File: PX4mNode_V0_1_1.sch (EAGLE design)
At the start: 135 parts, among them J201 DF13C-6P-1.25V, J202 DF13C-6P-1.25V, J203 DF13C-6P-1.25V, J301 DF13C-4P-1.25V, J401 DF13C-7P-1.25V, J402 DF13-4P-1.25V, J403 DF13C-4P-1.25V, J404 DF13C-4P-1.25V, J405 DF13C-4P-1.25V, J801 DF13C-3P-1.25V, M3_MOUNT1101 MOUNT-HOLE3.1MM, M3_MOUNT1102 MOUNT-HOLE3.1MM, M3_MOUNT1103 MOUNT-HOLE3.1MM, M3_MOUNT1104 MOUNT-HOLE3.1MM, U101 STM32F4X7VX, U401 MAX3051, U402 MAX3051, X101 3.2x2.5 mm / 24 MHz / 15 ppm

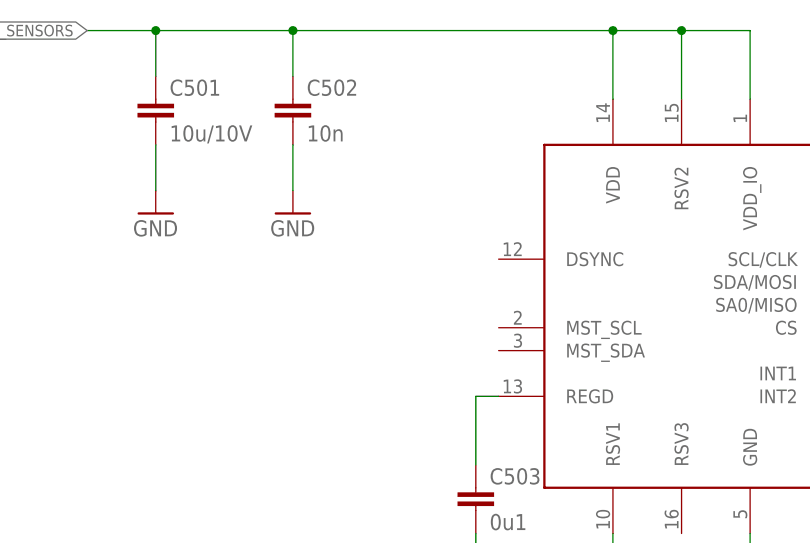
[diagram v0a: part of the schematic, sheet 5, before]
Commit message: Patched MAX21100 DRDY to MAG_DRDY
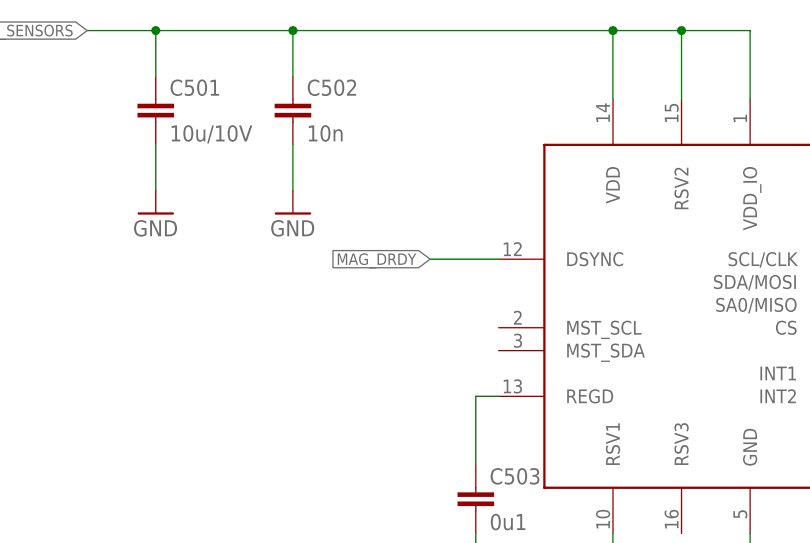
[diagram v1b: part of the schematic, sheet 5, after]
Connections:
- net MAG_DRDY: now also U$501.DSYNC
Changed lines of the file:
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@@
+</segment>
+</net>
+<net name="MAG_DRDY" class="0">
+<segment>
+<pinref part="U$501" gate="A" pin="DSYNC"/>
+<wire x1="88.9" y1="76.2" x2="81.28" y2="76.2" width="0.1524" layer="91"/>
+<label x="81.28" y="76.2" size="1.27" layer="95" rot="R180" xref="yes"/>
 </segment>
 </net>

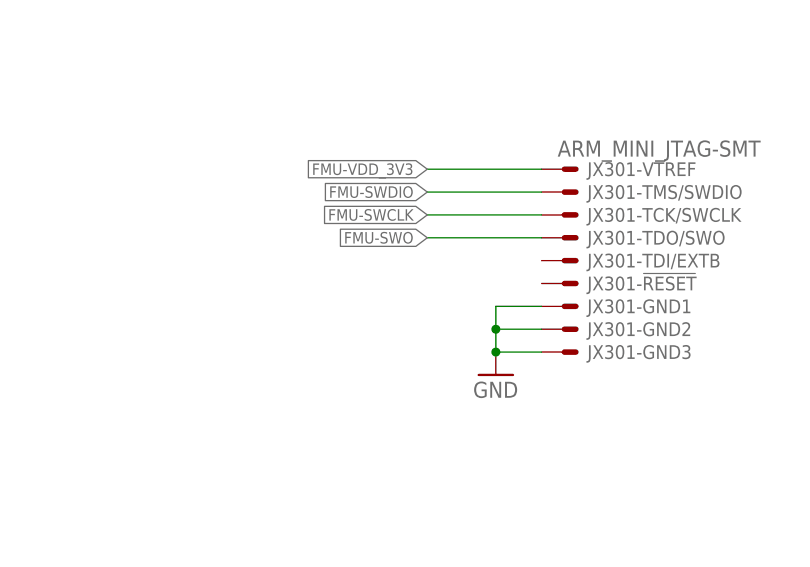
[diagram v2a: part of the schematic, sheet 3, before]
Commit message: Added nReset SWD connection to !FMU_RESET
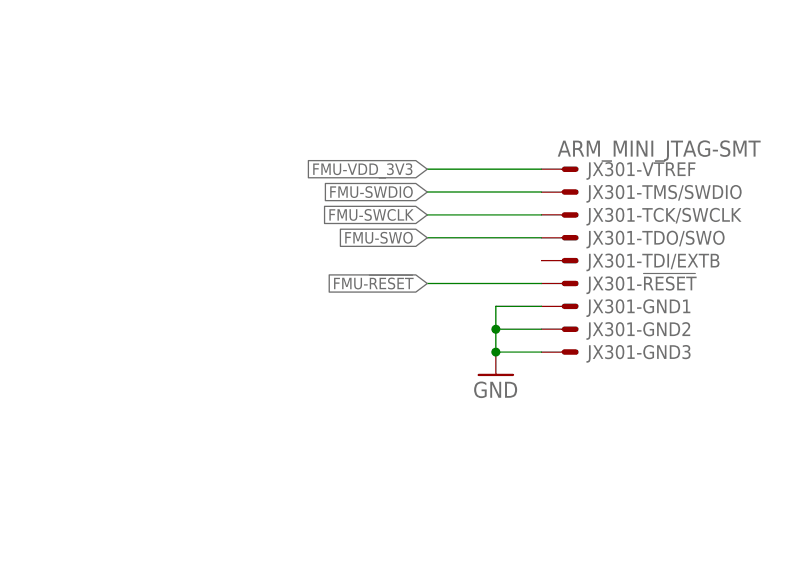
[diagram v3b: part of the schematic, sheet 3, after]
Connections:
- net FMU-!RESET: now also JX301-!RESET.S
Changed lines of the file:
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@@
+</segment>
+</net>
+<net name="FMU-!RESET" class="0">
+<segment>
+<label x="185.42" y="86.36" size="1.27" layer="95" rot="R180" xref="yes"/>
+<pinref part="JX301" gate="-!RESET" pin="S"/>
+<wire x1="185.42" y1="86.36" x2="198.12" y2="86.36" width="0.1524" layer="91"/>
 </segment>
 </net>

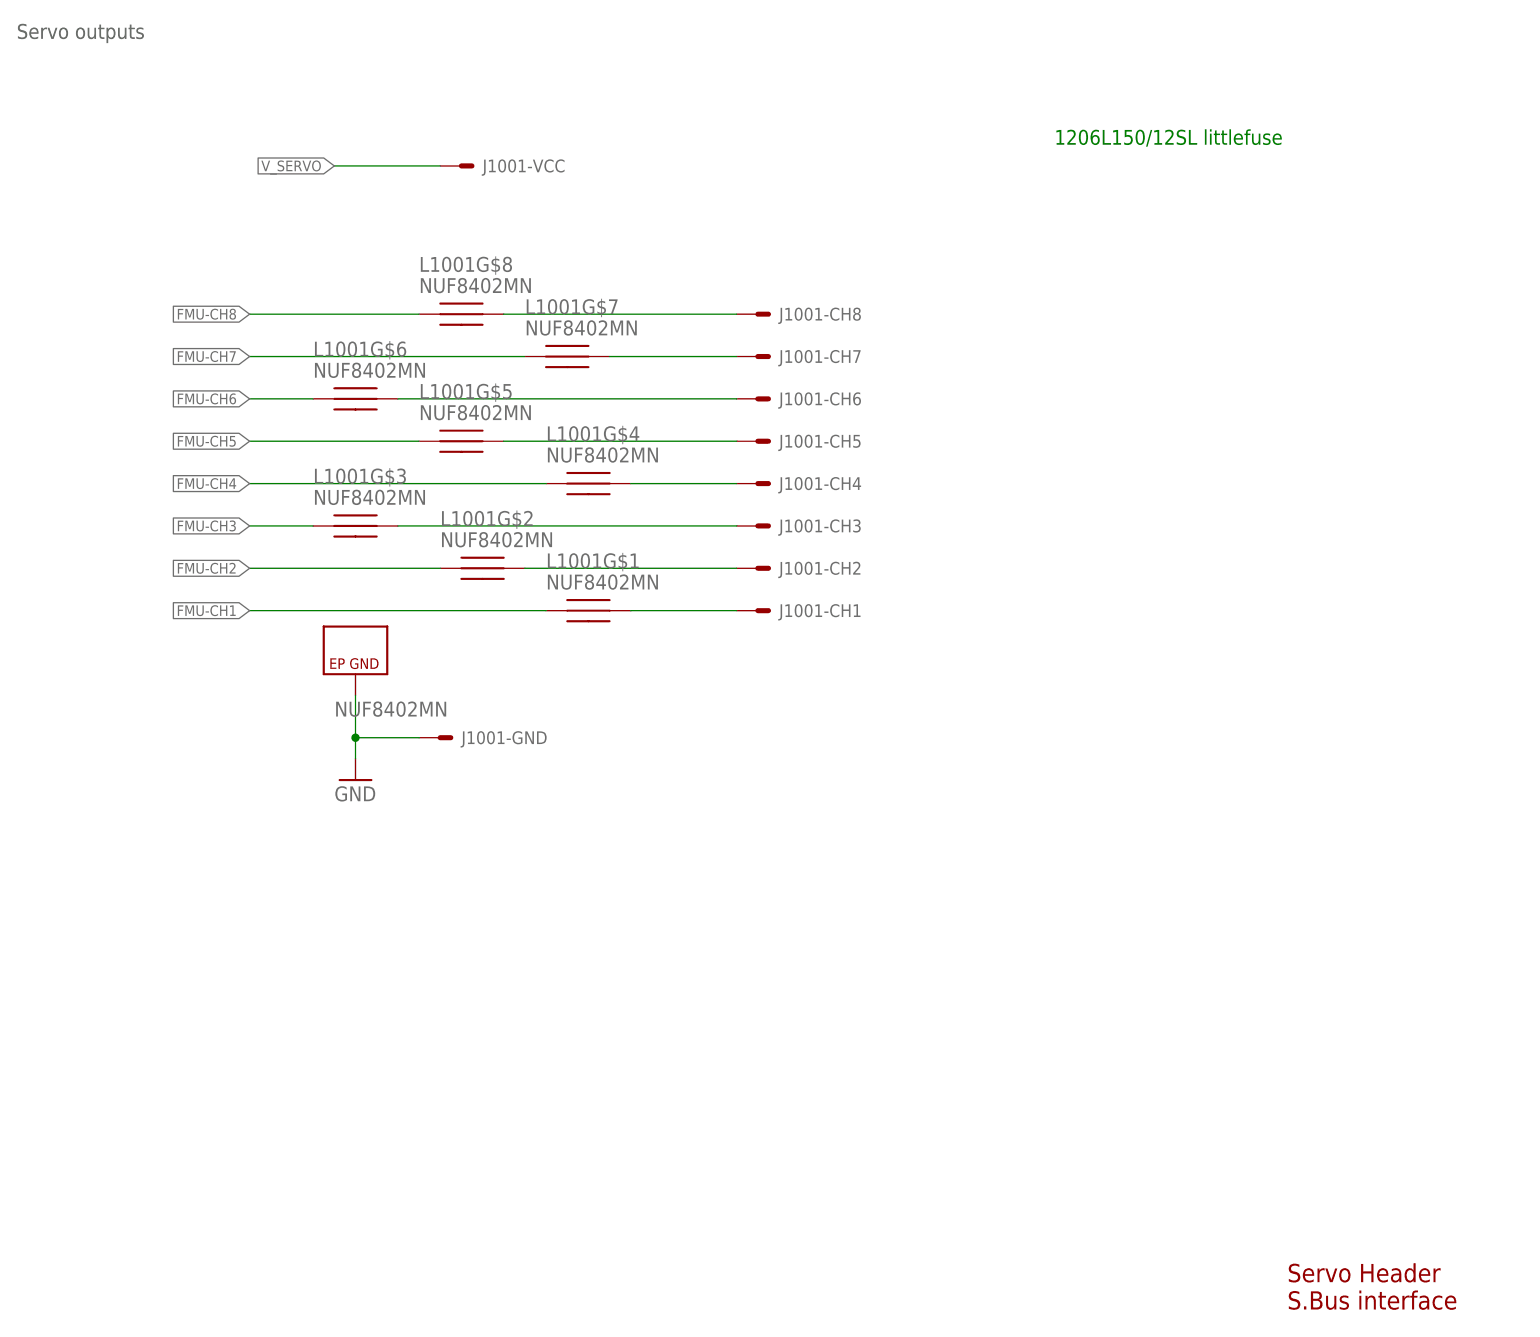
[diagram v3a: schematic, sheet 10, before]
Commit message: Added extra ground and power connections
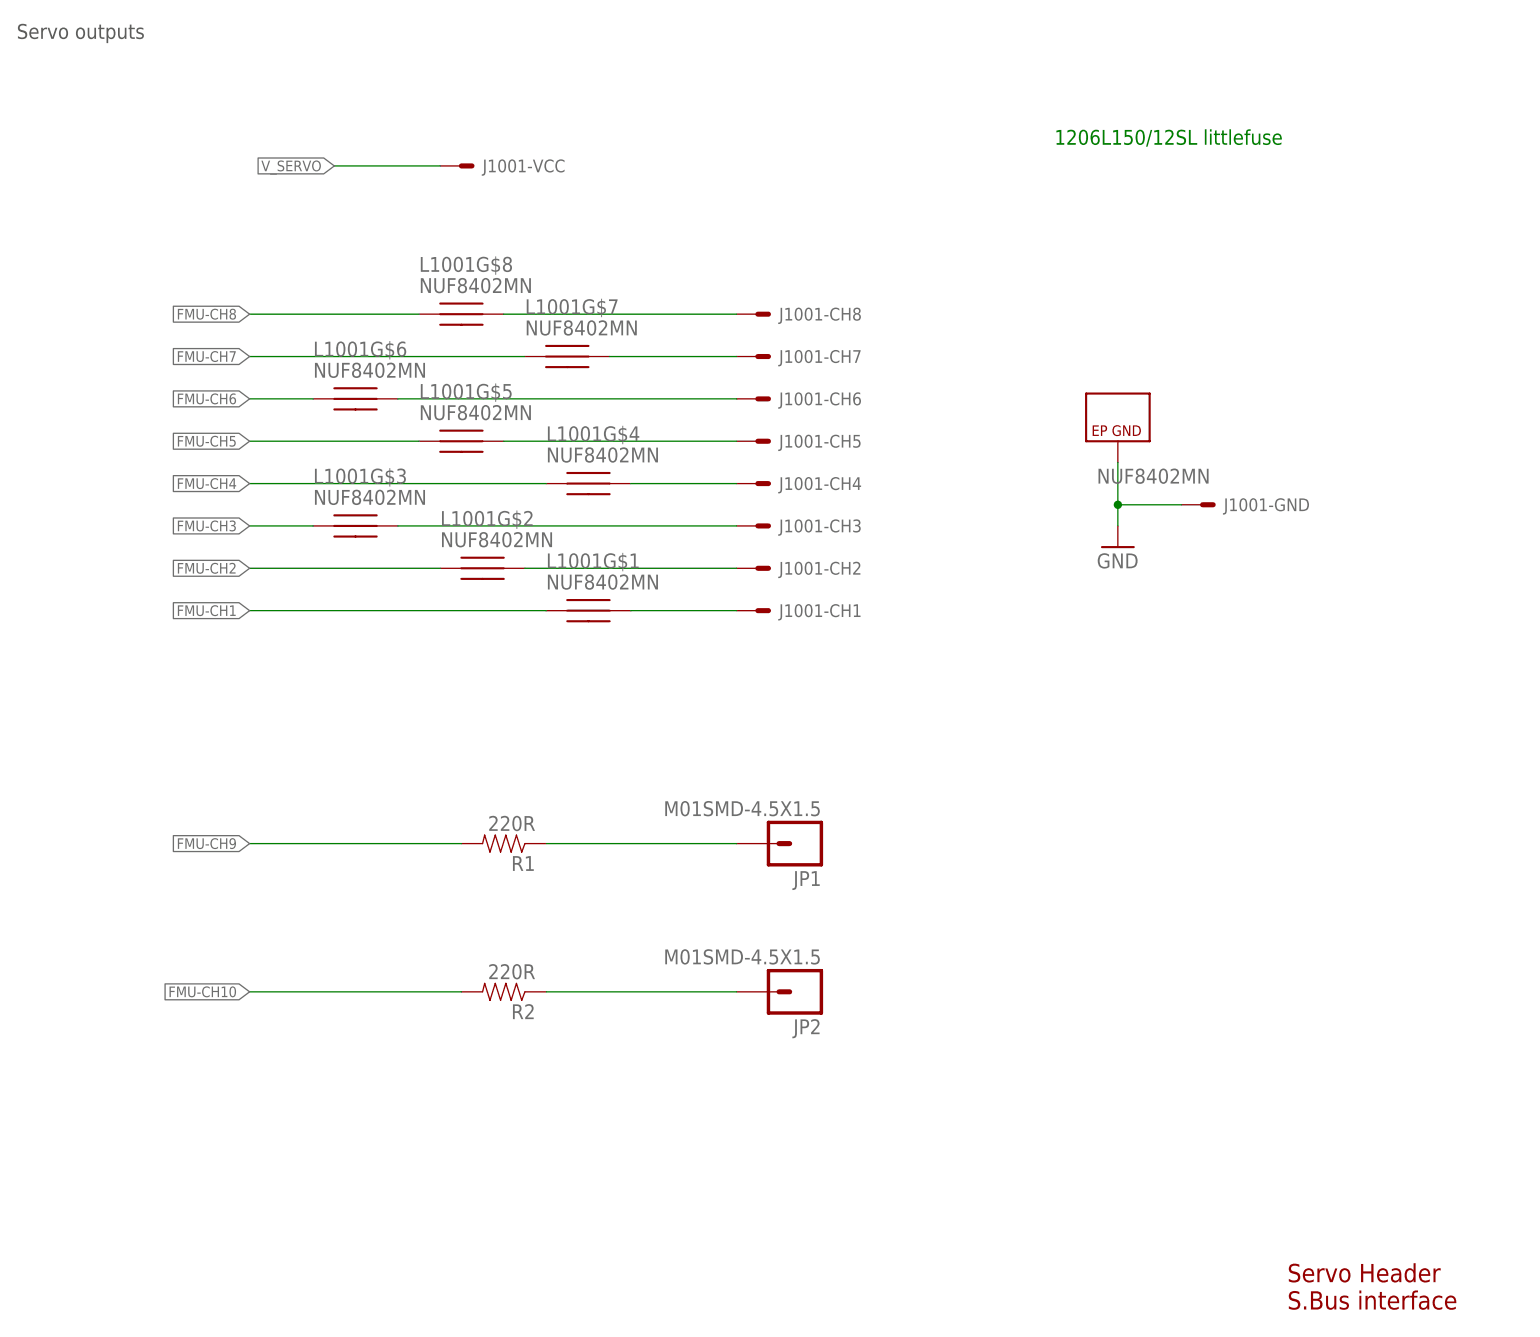
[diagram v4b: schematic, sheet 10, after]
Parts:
- added JP1, JP2, JP3: M01SMD-4.5X1.5, SparkFun-Connectors:M01SMD-4.5X1.5
- added R1, R2: 220R, pixhawk2:RESISTOR0402-RES
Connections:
- new net N$19: JP1.1, R1.1
- new net N$23: JP2.1, R2.1
- net FMU-CH10: now also R2.2
- net FMU-CH9: now also R1.2
- net GND: now also JP3.1
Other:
- moved on the sheet: J1001-GND, JP701
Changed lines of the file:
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@@
 <attribute name="PARTNO" value="MSS1P4-M3/89A"/>
 </part>
+<part name="JP1" library="SparkFun-Connectors" deviceset="M01" device="SMD-4.5X1.5"/>
+<part name="JP2" library="SparkFun-Connectors" deviceset="M01" device="SMD-4.5X1.5"/>
+<part name="R1" library="pixhawk2" deviceset="RESISTOR" device="0402-RES" value="220R">
+<attribute name="PARTNO" value="RC0402FR-07220RL"/>
+</part>
+<part name="R2" library="pixhawk2" deviceset="RESISTOR" device="0402-RES" value="220R">
+<attribute name="PARTNO" value="RC0402FR-07220RL"/>
+</part>
+<part name="JP3" library="SparkFun-Connectors" deviceset="M01" device="SMD-4.5X1.5"/>
 </parts>
 <sheets>
@@
 <attribute name="PARTNO" x="170.18" y="157.48" size="1.778" layer="96" display="off"/>
 </instance>
-<instance part="JP701" gate="G$1" x="190.5" y="101.6"/>
+<instance part="JP701" gate="G$1" x="195.58" y="104.14"/>
 <instance part="D701" gate="G$1" x="205.74" y="127" smashed="yes" rot="MR270">
 <attribute name="NAME" x="210.3374" y="127" size="1.778" layer="95" rot="MR270"/>
 <attribute name="PARTNO" x="205.74" y="127" size="1.778" layer="96" rot="MR90" display="off"/>
 </instance>
+<instance part="JP3" gate="G$1" x="195.58" y="91.44"/>
 </instances>
 <busses>
@@
 <wire x1="233.68" y1="91.44" x2="233.68" y2="96.52" width="0.1524" layer="91"/>
 <junction x="223.52" y="91.44"/>
+<pinref part="JP3" gate="G$1" pin="1"/>
+<wire x1="203.2" y1="91.44" x2="223.52" y2="91.44" width="0.1524" layer="91"/>
 </segment>
 <segment>
@@
 <junction x="205.74" y="111.76"/>
 <wire x1="213.36" y1="111.76" x2="233.68" y2="111.76" width="0.1524" layer="91"/>
-<wire x1="205.74" y1="111.76" x2="195.58" y2="111.76" width="0.1524" layer="91"/>
-<label x="195.58" y="111.76" size="1.27" layer="95" rot="R180" xref="yes"/>
+<wire x1="205.74" y1="111.76" x2="185.42" y2="111.76" width="0.1524" layer="91"/>
+<label x="185.42" y="111.76" size="1.27" layer="95" rot="R180" xref="yes"/>
 <pinref part="R706" gate="G$1" pin="1"/>
 <pinref part="JP701" gate="G$1" pin="1"/>
-<wire x1="198.12" y1="101.6" x2="213.36" y2="101.6" width="0.1524" layer="91"/>
-<wire x1="213.36" y1="101.6" x2="213.36" y2="111.76" width="0.1524" layer="91"/>
+<wire x1="203.2" y1="104.14" x2="213.36" y2="104.14" width="0.1524" layer="91"/>
+<wire x1="213.36" y1="104.14" x2="213.36" y2="111.76" width="0.1524" layer="91"/>
 <junction x="213.36" y="111.76"/>
 </segment>
@@
 <instance part="L1001" gate="G$7" x="78.74" y="129.54"/>
 <instance part="L1001" gate="G$8" x="66.04" y="134.62"/>
-<instance part="GND5" gate="1" x="53.34" y="78.74"/>
-<instance part="L1001" gate="G$9" x="53.34" y="88.9"/>
-<instance part="J1001" gate="-GND" x="63.5" y="83.82"/>
+<instance part="GND5" gate="1" x="144.78" y="106.68"/>
+<instance part="L1001" gate="G$9" x="144.78" y="116.84"/>
+<instance part="J1001" gate="-GND" x="154.94" y="111.76"/>
 <instance part="J1001" gate="-VCC" x="66.04" y="152.4"/>
 <instance part="J1001" gate="-CH1" x="101.6" y="99.06"/>
@@
 <instance part="J1001" gate="-CH7" x="101.6" y="129.54"/>
 <instance part="J1001" gate="-CH8" x="101.6" y="134.62"/>
+<instance part="JP1" gate="G$1" x="106.68" y="71.12" rot="R180"/>
+<instance part="JP2" gate="G$1" x="106.68" y="53.34" rot="R180"/>
+<instance part="R1" gate="G$1" x="71.12" y="71.12" rot="R180">
+<attribute name="PARTNO" x="71.12" y="71.12" size="1.778" layer="96" rot="R90" display="off"/>
+</instance>
+<instance part="R2" gate="G$1" x="71.12" y="53.34" rot="R180">
+<attribute name="PARTNO" x="71.12" y="53.34" size="1.778" layer="96" rot="R90" display="off"/>
+</instance>
 </instances>
 <busses>
@@
 <segment>
 <pinref part="GND5" gate="1" pin="GND"/>
-<wire x1="53.34" y1="81.28" x2="53.34" y2="83.82" width="0.1524" layer="91"/>
+<wire x1="144.78" y1="109.22" x2="144.78" y2="111.76" width="0.1524" layer="91"/>
 <pinref part="L1001" gate="G$9" pin="GND"/>
 <pinref part="J1001" gate="-GND" pin="S"/>
-<wire x1="53.34" y1="83.82" x2="53.34" y2="88.9" width="0.1524" layer="91"/>
-<wire x1="60.96" y1="83.82" x2="53.34" y2="83.82" width="0.1524" layer="91"/>
-<junction x="53.34" y="83.82"/>
+<wire x1="144.78" y1="111.76" x2="144.78" y2="116.84" width="0.1524" layer="91"/>
+<wire x1="152.4" y1="111.76" x2="144.78" y2="111.76" width="0.1524" layer="91"/>
+<junction x="144.78" y="111.76"/>
 </segment>
 </net>
@@
 </segment>
 </net>
+<net name="N$19" class="0">
+<segment>
+<pinref part="JP1" gate="G$1" pin="1"/>
+<pinref part="R1" gate="G$1" pin="1"/>
+<wire x1="99.06" y1="71.12" x2="76.2" y2="71.12" width="0.1524" layer="91"/>
+</segment>
+</net>
+<net name="N$23" class="0">
+<segment>
+<pinref part="JP2" gate="G$1" pin="1"/>
+<pinref part="R2" gate="G$1" pin="1"/>
+<wire x1="99.06" y1="53.34" x2="76.2" y2="53.34" width="0.1524" layer="91"/>
+</segment>
+</net>
+<net name="FMU-CH9" class="0">
+<segment>
+<wire x1="40.64" y1="71.12" x2="66.04" y2="71.12" width="0.1524" layer="91"/>
+<label x="40.64" y="71.12" size="1.27" layer="95" rot="R180" xref="yes"/>
+<pinref part="R1" gate="G$1" pin="2"/>
+</segment>
+</net>
+<net name="FMU-CH10" class="0">
+<segment>
+<label x="40.64" y="53.34" size="1.27" layer="95" rot="R180" xref="yes"/>
+<wire x1="40.64" y1="53.34" x2="66.04" y2="53.34" width="0.1524" layer="91"/>
+<pinref part="R2" gate="G$1" pin="2"/>
+</segment>
+</net>

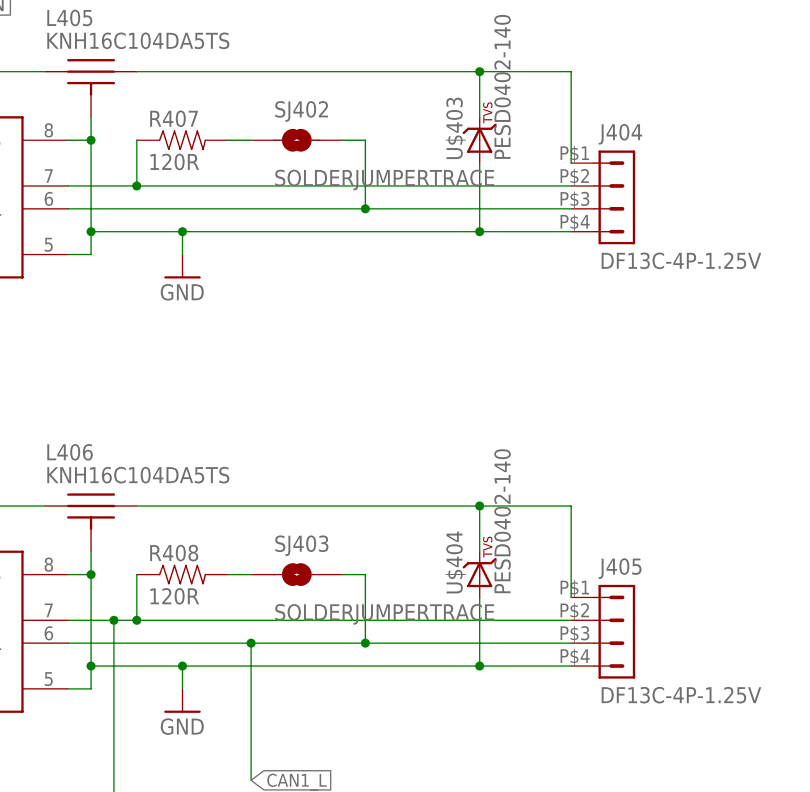
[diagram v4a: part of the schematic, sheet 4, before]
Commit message: Stop mask removed from vias
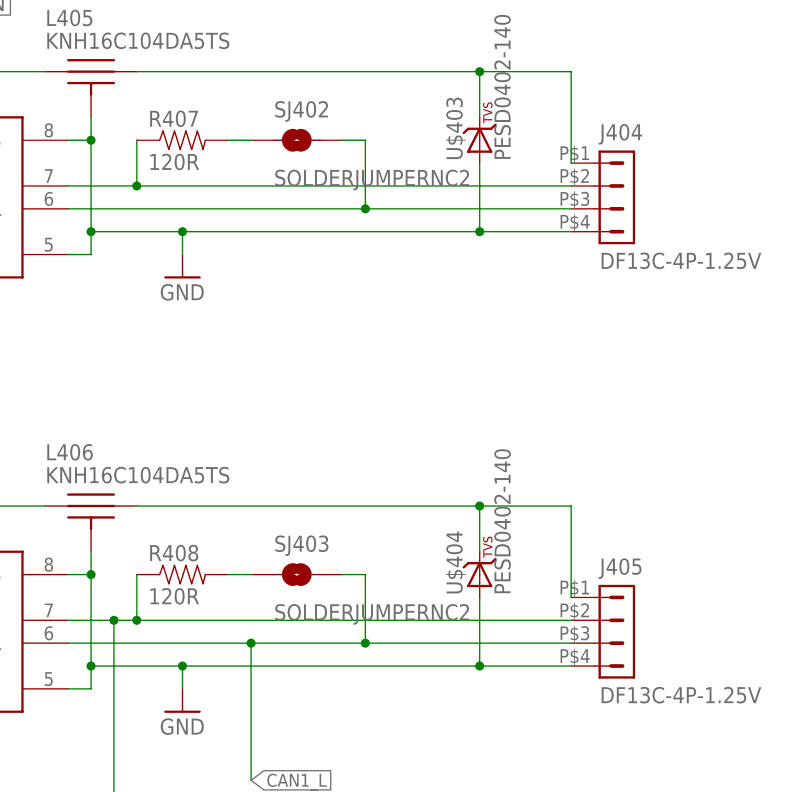
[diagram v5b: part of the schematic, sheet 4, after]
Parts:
- SJ402, SJ403: value SOLDERJUMPERTRACE -> SOLDERJUMPERNC2; device SparkFun-Passives:SOLDERJUMPERTRACE -> SparkFun-Passives:SOLDERJUMPERNC2
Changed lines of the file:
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@@
 <part name="GND17" library="pixhawk2" deviceset="GND" device=""/>
 <part name="L402" library="PX4lite" deviceset="NUF8402MN" device=""/>
-<part name="SJ403" library="SparkFun-Passives" deviceset="SOLDERJUMPER" device="TRACE"/>
+<part name="SJ403" library="SparkFun-Passives" deviceset="SOLDERJUMPER" device="NC2" value="SOLDERJUMPERNC2"/>
 <part name="J$401" library="PX4lite" deviceset="HEADER-3X1" device="BOARDEDGE-SHORT"/>
 <part name="C403" library="pixhawk2" deviceset="CAP" device="0402" value="0u1">
@@
 <attribute name="PARTNO" value="PESD0402-140"/>
 </part>
-<part name="SJ402" library="SparkFun-Passives" deviceset="SOLDERJUMPER" device="TRACE"/>
+<part name="SJ402" library="SparkFun-Passives" deviceset="SOLDERJUMPER" device="NC2" value="SOLDERJUMPERNC2"/>
 <part name="U$501" library="PX4lite" deviceset="MAX21100" device=""/>
 <part name="C503" library="pixhawk2" deviceset="CAP" device="0402" value="0u1">
